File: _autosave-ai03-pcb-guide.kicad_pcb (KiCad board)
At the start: 2 copper layers, 24 parts, among them SW1 SW_Push, U1 ATmega32U4-AU, Y1 16MHz

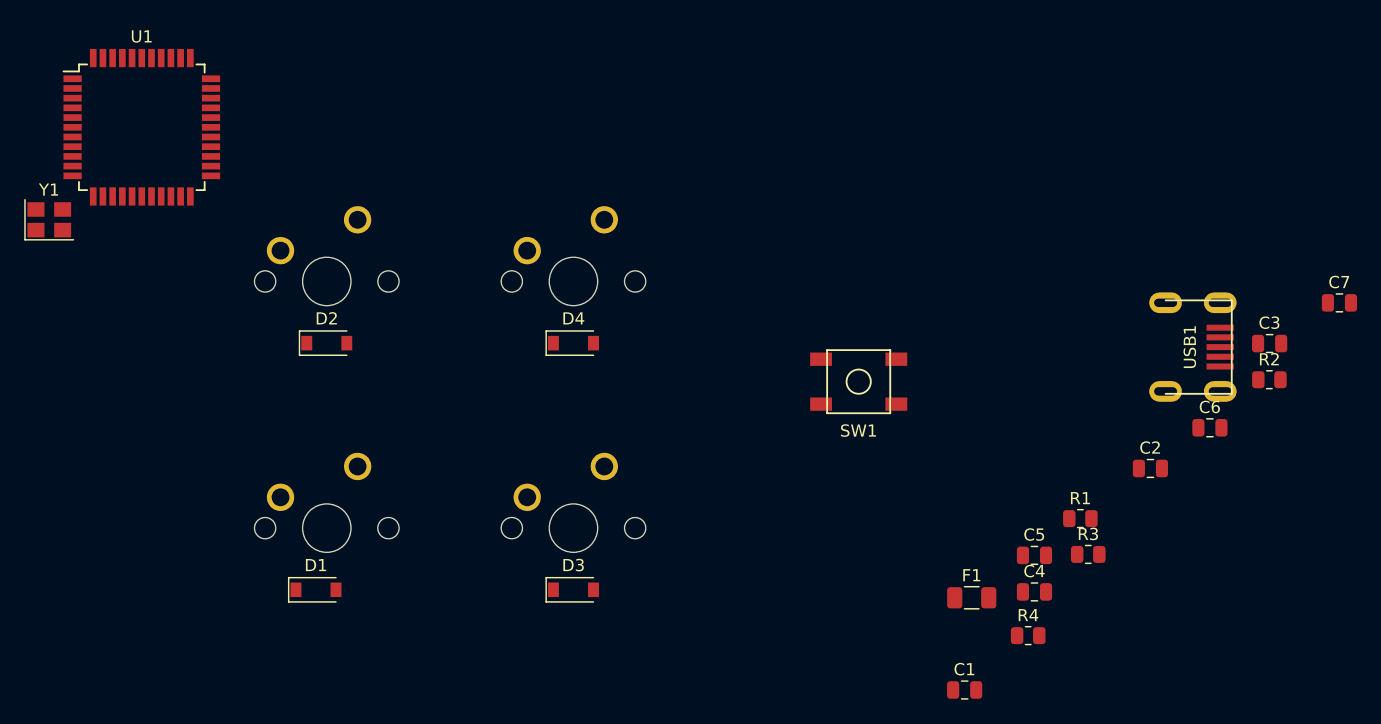
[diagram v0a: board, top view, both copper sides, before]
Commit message: finished PCB compnent placements and routing
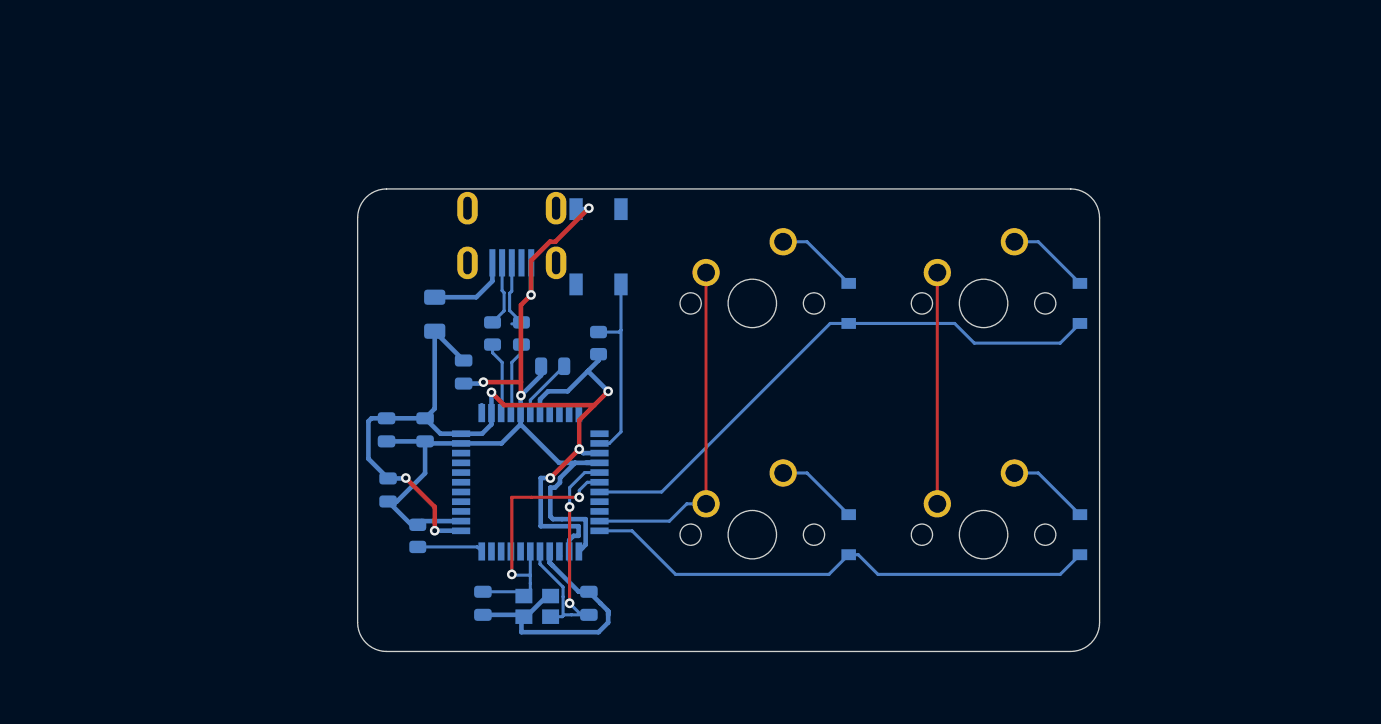
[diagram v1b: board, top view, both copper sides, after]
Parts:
- C1, C2, C3, C4, C5, C6, C7, D1, D2, D3, D4, F1, R1, R2, R3, R4, SW1, U1, USB1, Y1: moved to B.Cu
- moved C7 65.0 mm to (54.2, 40.0), turned to 180 degrees
- moved C6 64.7 mm to (43.7, 45.2), turned to 270 degrees
- moved R2 61.7 mm to (51.6, 37.3), turned to 90 degrees
- moved C3 60.0 mm to (57.1, 59.5), turned to 90 degrees
- moved C2 56.1 mm to (48.4, 59.5), turned to 270 degrees
- moved USB1 55.1 mm to (50.8, 27.0), turned to 270 degrees
- moved C5 54.4 mm to (40.5, 45.2), turned to 270 degrees
- moved Y1 51.3 mm to (52.9, 59.8)
- moved R4 51.0 mm to (43.1, 54.0), turned to 270 degrees
- moved R1 50.8 mm to (49.2, 37.3), turned to 90 degrees
- moved C4 50.4 mm to (46.8, 40.5), turned to 270 degrees
- moved C1 50.3 mm to (40.6, 50.2), turned to 270 degrees
- moved F1 50.0 mm to (44.5, 35.7), turned to 90 degrees
- moved D3 47.9 mm to (97.6, 34.8), turned to 90 degrees
- moved D4 44.6 mm to (97.6, 53.9), turned to 90 degrees
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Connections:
- U1 pad 18: Net-(U1-Pad18) -> ROW0
- U1 pad 20: Net-(U1-Pad20) -> COL1
- U1 pad 21: Net-(U1-Pad21) -> COL0
- U1 pad 22: Net-(U1-Pad22) -> ROW1
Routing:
- net GND: track 0.00 -> 104.9 mm, vias 0 -> 4
- net +5V: track 0.00 -> 80.3 mm, vias 0 -> 6
- net ROW0: track 0.00 -> 46.7 mm
- net ROW1: track 0.00 -> 43.1 mm
- net COL0: track 0.00 -> 28.4 mm
- net Net-(C3-Pad1): track 0.00 -> 23.8 mm, vias 0 -> 2
- net Net-(C2-Pad1): track 0.00 -> 23.4 mm, vias 0 -> 2
- net COL1: track 0.00 -> 19.1 mm
- net Net-(R3-Pad2): track 0.00 -> 16.2 mm
- net D+: track 0.00 -> 7.31 mm
- net VCC: track 0.00 -> 6.99 mm
- net Net-(D4-Pad2): track 0.00 -> 6.82 mm
- net Net-(D3-Pad2): track 0.00 -> 6.82 mm
- net Net-(D2-Pad2): track 0.00 -> 6.82 mm
- net Net-(D1-Pad2): track 0.00 -> 6.82 mm
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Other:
- board outline added: 61.1 x 38.1 mm
- net class Default: trace_width 0.25 -> 0.254
- net class Power added: clearance 0.2, trace_width 0.381, via_dia 0.8, via_drill 0.4
